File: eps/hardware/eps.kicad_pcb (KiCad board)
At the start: 4 copper layers, 80 x 80 mm, 401 parts, among them J1 USB_C_Receptacle_USB2.0_16P, J10 Conn_02x20_Counter_Clockwise, J11 Conn_01x03, J12 Conn_01x03, J13 Conn_ARM_JTAG_SWD_10, J2 Conn_01x02, J3 Conn_01x02, J4 Conn_01x02, J5 Conn_01x02, J6 Conn_01x02, J7 Conn_01x02, J8 Conn_01x02, Q1 NMOS, Q10 IRLML0030, Q11 IRLML0030, Q12 IRLML0030, Q13 IRLML0030, Q14 IRLML0030, Q15 IRLML0030, Q16 IRLML0030, Q17 IRLML0030, Q18 IRLML0030, Q19 IRLML0030, Q2 NMOS, Q20 IRLML0030, Q3 NMOS, Q4 NMOS, Q5 IRLML0030, Q6 IRLML0030, Q7 IRLML0030, Q8 IRLML0030, Q9 IRLML0030, SW1 SW_Push, SW2 SW_SPDT, U1 TPS22810DRV, U10 STM32L496ZGTx, U11 NCS214RSQT2G, U12 74LVC1G07SE-7, U14 TPS22810DRVT, U15 NCS214RSQT2G, U16 74LVC1G07SE-7, U18 TPS22810DRVT, U19 NCS214RSQT2G, U2 LTC3130-1, U20 74LVC1G07SE-7, U22 TPS22810DRVT, U23 NCS214RSQT2G, U24 74LVC1G07SE-7, U26 TPS22810DRVT, U27 NCS214RSQT2G, U28 74LVC1G07SE-7, U3 LTC4162-L, U30 TPS22810DRVT, U31 NCS214RSQT2G, U32 74LVC1G07SE-7, U34 TPS22810DRVT, U35 NCS214RSQT2G, U36 74LVC1G07SE-7, U38 TPS22810DRVT, U39 MP28167-A, U4 LTC4162-L, U40 MP28167-A, U41 LTC4415, U42 LTC4415, U5 NCS214RSQT2G, U6 74LVC1G07SE-7, U8 TPS22810DRVT, U9 TPS35-Q1, Y1 8MHz, Y2 32KHz

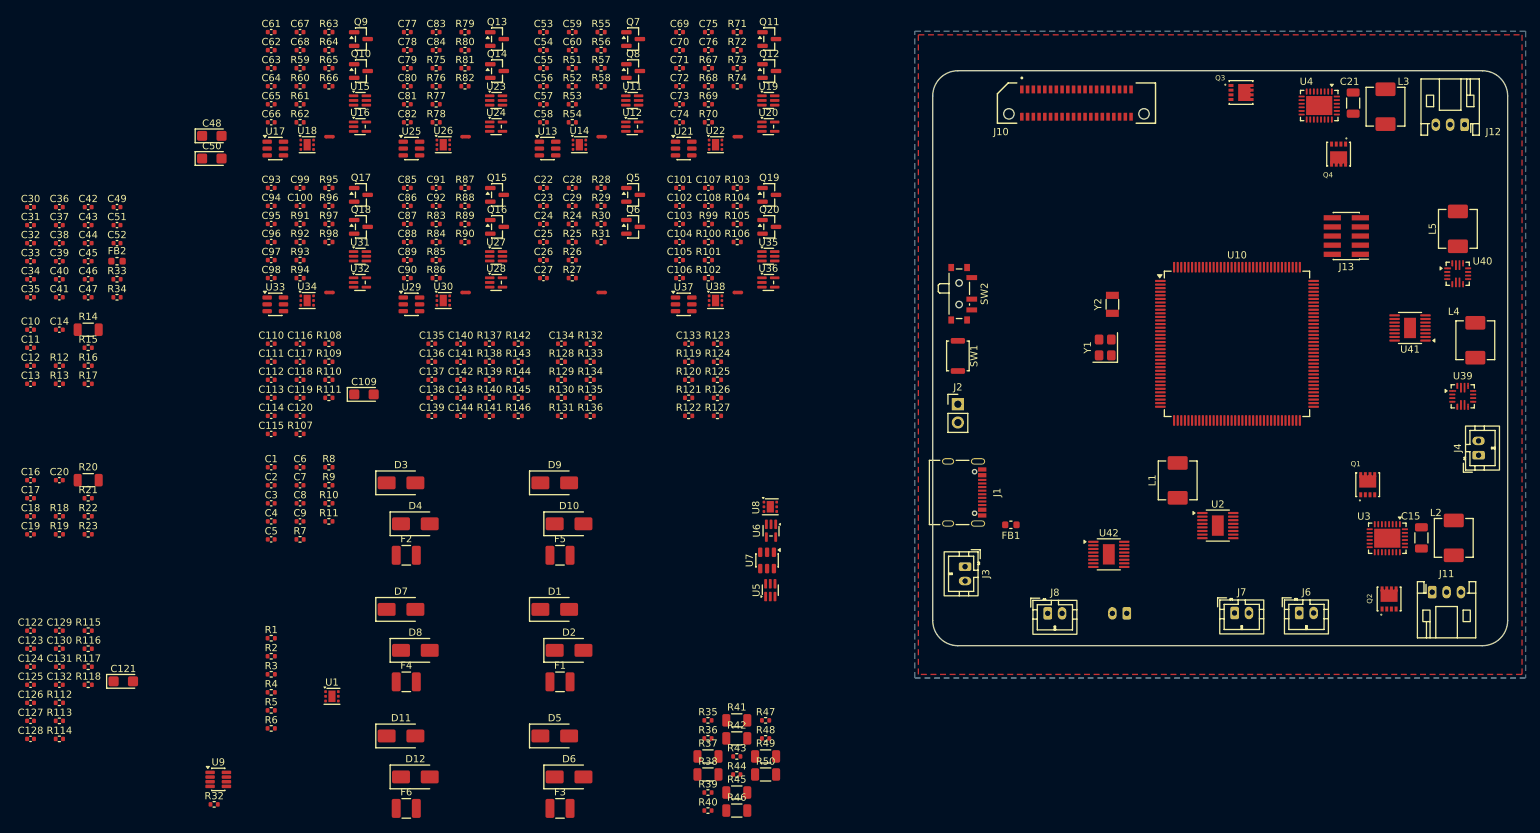
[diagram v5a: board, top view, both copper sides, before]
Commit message: start placement of one current monitor
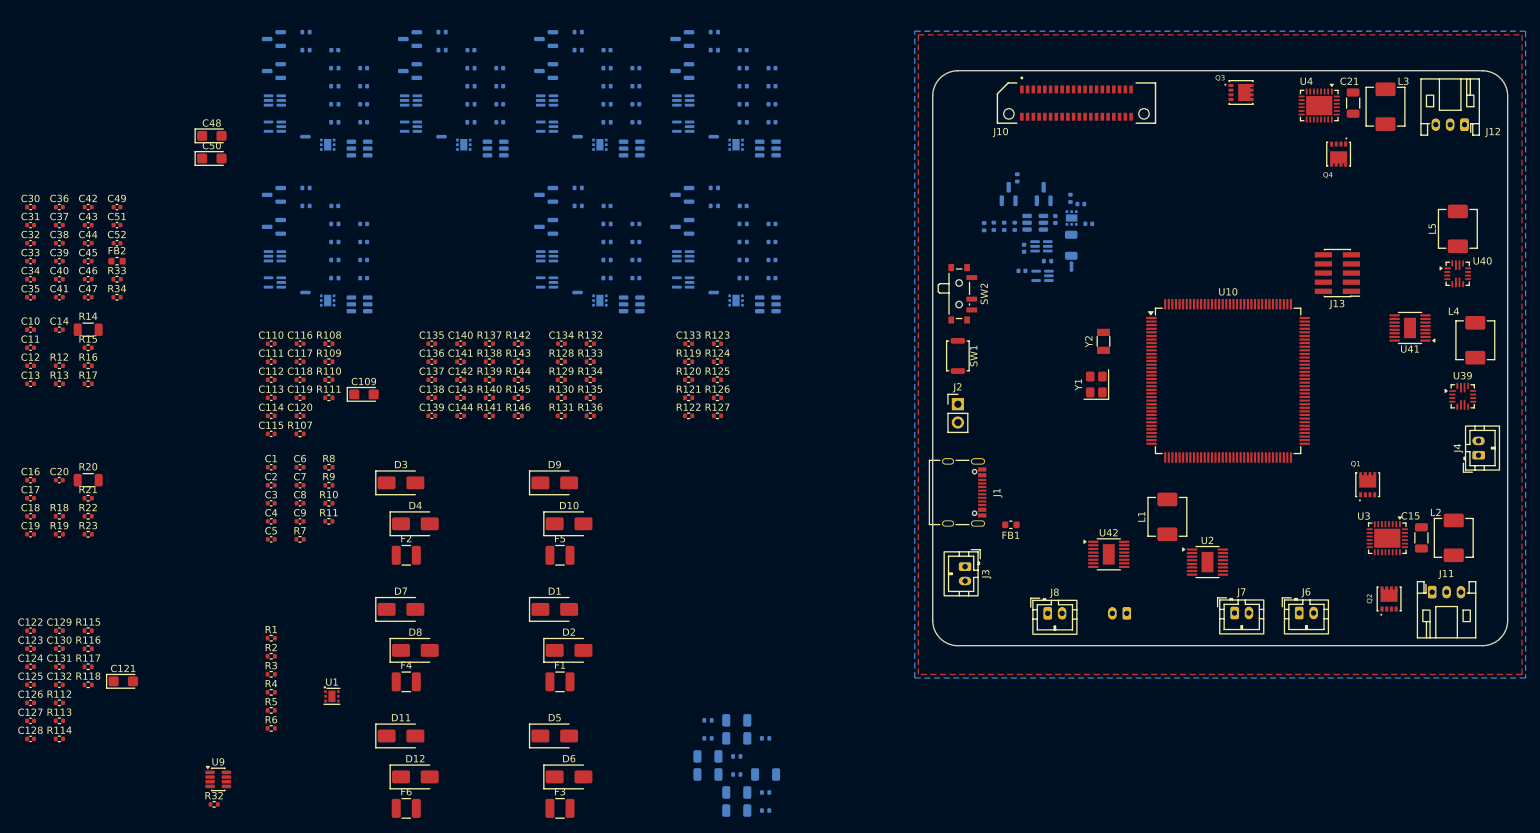
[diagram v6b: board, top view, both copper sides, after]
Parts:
- removed C101, C102, C107, C22, C23, C28, C53, C54, C59, C61, C62, C67, C69, C70, C75, C77, C78, C83, C85, C86, C91, C93, C94, C99: ~, Capacitor_SMD:C_0402_1005Metric
- removed R105, R106, R30, R31, R57, R58, R65, R66, R73, R74, R81, R82, R89, R90, R97, R98: 0, Resistor_SMD:R_0402_1005Metric
- C100, C103, C104, C105, C106, C108, C24, C25, C26, C27, C29, C55, C56, C57, C58, C60, C63, C64, C65, C66, C68, C71, C72, C73, C74, C76, C79, C80, C81, C82, C84, C87, C88, C89, C90, C92, C95, C96, C97, C98, NT1, NT2, NT3, NT4, NT5, NT6, NT7, NT8, Q10, Q11, Q12, Q13, Q14, Q15, Q16, Q17, Q18, Q19, Q20, Q5, Q6, Q7, Q8, Q9, R100, R101, R102, R103, R104, R24, R25, R26, R27, R28, R29, R35, R36, R37, R38, R39, R40, R41, R42, R43, R44, R45, R46, R47, R48, R49, R50, R51, R52, R53, R54, R55, R56, R59, R60, R61, R62, R63, R64, R67, R68, R69, R70, R71, R72, R75, R76, R77, R78, R79, R80, R83, R84, R85, R86, R87, R88, R91, R92, R93, R94, R95, R96, R99, U11, U12, U13, U14, U15, U16, U17, U18, U19, U20, U21, U22, U23, U24, U25, U26, U27, U28, U29, U30, U31, U32, U33, U34, U35, U36, U37, U38, U5, U6, U7, U8: moved to B.Cu
- moved R37 87.3 mm to (180.3, 76.3), turned to 90 degrees
- moved R35 80.9 mm to (172.4, 73.7), turned to -90 degrees
- moved C27 75.5 mm to (181.6, 70.5), turned to 180 degrees
- moved C29 71.9 mm to (182.7, 73.3), turned to 180 degrees
- moved C26 71.5 mm to (178.1, 72.7), turned to 90 degrees
- moved C63 69.7 mm to (138.6, 51.6), turned to 180 degrees
- moved C64 69.7 mm to (138.6, 54.1), turned to 180 degrees
- moved C65 69.7 mm to (138.6, 56.7), turned to 180 degrees
- moved C66 69.7 mm to (138.6, 59.2), turned to 180 degrees
- moved C95 69.7 mm to (138.6, 73.3), turned to 180 degrees
- moved C96 69.7 mm to (138.6, 75.8), turned to 180 degrees
- moved C97 69.7 mm to (138.6, 78.3), turned to 180 degrees
- moved C98 69.7 mm to (138.6, 80.8), turned to 180 degrees
- moved Q11 68.9 mm to (69.3, 47.6), turned to 180 degrees
- moved Q12 68.9 mm to (69.3, 52.0), turned to 180 degrees
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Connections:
- C103 pad 1: Net-(U37-VDD) -> /Current Monitors/RAIL_8_VOUT
- C104 pad 2: Net-(U37-VDD) -> /Current Monitors/RAIL_8_VOUT
- C24 pad 1: Net-(U7-VDD) -> /Current Monitors/RAIL_1_VOUT
- C25 pad 2: Net-(U7-VDD) -> /Current Monitors/RAIL_1_VOUT
- C55 pad 1: Net-(U13-VDD) -> /Current Monitors/RAIL_2_VOUT
- C56 pad 2: Net-(U13-VDD) -> /Current Monitors/RAIL_2_VOUT
- C63 pad 1: Net-(U17-VDD) -> /Current Monitors/RAIL_3_VOUT
- C64 pad 2: Net-(U17-VDD) -> /Current Monitors/RAIL_3_VOUT
- C71 pad 1: Net-(U21-VDD) -> /Current Monitors/RAIL_4_VOUT
- C72 pad 2: Net-(U21-VDD) -> /Current Monitors/RAIL_4_VOUT
- C79 pad 1: Net-(U25-VDD) -> /Current Monitors/RAIL_5_VOUT
- C80 pad 2: Net-(U25-VDD) -> /Current Monitors/RAIL_5_VOUT
- C87 pad 1: Net-(U29-VDD) -> /Current Monitors/RAIL_6_VOUT
- C88 pad 2: Net-(U29-VDD) -> /Current Monitors/RAIL_6_VOUT
- C95 pad 1: Net-(U33-VDD) -> /Current Monitors/RAIL_7_VOUT
- C96 pad 2: Net-(U33-VDD) -> /Current Monitors/RAIL_7_VOUT
- R139 pad 1: /Current Monitors/RAIL_1_ADC -> GND
- R140 pad 1: /Current Monitors/RAIL_2_ADC -> GND
- R141 pad 1: /Current Monitors/RAIL_3_ADC -> GND
- R142 pad 1: /Current Monitors/RAIL_4_ADC -> GND
- R143 pad 1: /Current Monitors/RAIL_5_ADC -> GND
- R144 pad 1: /Current Monitors/RAIL_6_ADC -> GND
- R145 pad 1: /Current Monitors/RAIL_7_ADC -> GND
- R146 pad 1: /Current Monitors/RAIL_8_ADC -> GND
- R24 pad 2: Net-(U7-VDD) -> /Current Monitors/RAIL_1_VOUT
- R51 pad 2: Net-(U13-VDD) -> /Current Monitors/RAIL_2_VOUT
- R59 pad 2: Net-(U17-VDD) -> /Current Monitors/RAIL_3_VOUT
- R67 pad 2: Net-(U21-VDD) -> /Current Monitors/RAIL_4_VOUT
- R75 pad 2: Net-(U25-VDD) -> /Current Monitors/RAIL_5_VOUT
- R83 pad 2: Net-(U29-VDD) -> /Current Monitors/RAIL_6_VOUT
- R91 pad 2: Net-(U33-VDD) -> /Current Monitors/RAIL_7_VOUT
- R99 pad 2: Net-(U37-VDD) -> /Current Monitors/RAIL_8_VOUT
- U11 pad 6: /Current Monitors/RAIL_2_ADC -> GND
- U12 pad 5: Net-(U13-VDD) -> /Current Monitors/RAIL_2_VOUT
- U13 pad 3: /Current Monitors/RAIL_2_ADC -> GND
- U13 pad 6: Net-(U13-VDD) -> /Current Monitors/RAIL_2_VOUT
- U14 pad 2: Net-(U14-QOD) -> /Current Monitors/RAIL_2_VOUT
- U14 pad 3: Net-(U14-CT) -> GND
- U15 pad 6: /Current Monitors/RAIL_3_ADC -> GND
- U16 pad 5: Net-(U17-VDD) -> /Current Monitors/RAIL_3_VOUT
- U17 pad 3: /Current Monitors/RAIL_3_ADC -> GND
- U17 pad 6: Net-(U17-VDD) -> /Current Monitors/RAIL_3_VOUT
- U18 pad 2: Net-(U18-QOD) -> /Current Monitors/RAIL_3_VOUT
- U18 pad 3: Net-(U18-CT) -> GND
- U19 pad 6: /Current Monitors/RAIL_4_ADC -> GND
- U20 pad 5: Net-(U21-VDD) -> /Current Monitors/RAIL_4_VOUT
- U21 pad 3: /Current Monitors/RAIL_4_ADC -> GND
- U21 pad 6: Net-(U21-VDD) -> /Current Monitors/RAIL_4_VOUT
- U22 pad 2: Net-(U22-QOD) -> /Current Monitors/RAIL_4_VOUT
- U22 pad 3: Net-(U22-CT) -> GND
- U23 pad 6: /Current Monitors/RAIL_5_ADC -> GND
- U24 pad 5: Net-(U25-VDD) -> /Current Monitors/RAIL_5_VOUT
- U25 pad 3: /Current Monitors/RAIL_5_ADC -> GND
- U25 pad 6: Net-(U25-VDD) -> /Current Monitors/RAIL_5_VOUT
- U26 pad 2: Net-(U26-QOD) -> /Current Monitors/RAIL_5_VOUT
- U26 pad 3: Net-(U26-CT) -> GND
- U27 pad 6: /Current Monitors/RAIL_6_ADC -> GND
- U28 pad 5: Net-(U29-VDD) -> /Current Monitors/RAIL_6_VOUT
- U29 pad 3: /Current Monitors/RAIL_6_ADC -> GND
- U29 pad 6: Net-(U29-VDD) -> /Current Monitors/RAIL_6_VOUT
- U30 pad 2: Net-(U30-QOD) -> /Current Monitors/RAIL_6_VOUT
- U30 pad 3: Net-(U30-CT) -> GND
- U31 pad 6: /Current Monitors/RAIL_7_ADC -> GND
- U32 pad 5: Net-(U33-VDD) -> /Current Monitors/RAIL_7_VOUT
- U33 pad 3: /Current Monitors/RAIL_7_ADC -> GND
- U33 pad 6: Net-(U33-VDD) -> /Current Monitors/RAIL_7_VOUT
- U34 pad 2: Net-(U34-QOD) -> /Current Monitors/RAIL_7_VOUT
- U34 pad 3: Net-(U34-CT) -> GND
- U35 pad 6: /Current Monitors/RAIL_8_ADC -> GND
- U36 pad 5: Net-(U37-VDD) -> /Current Monitors/RAIL_8_VOUT
- U37 pad 3: /Current Monitors/RAIL_8_ADC -> GND
- U37 pad 6: Net-(U37-VDD) -> /Current Monitors/RAIL_8_VOUT
- U38 pad 2: Net-(U38-QOD) -> /Current Monitors/RAIL_8_VOUT
- U38 pad 3: Net-(U38-CT) -> GND
- U5 pad 6: /Current Monitors/RAIL_1_ADC -> GND
- U6 pad 5: Net-(U7-VDD) -> /Current Monitors/RAIL_1_VOUT
- U7 pad 3: /Current Monitors/RAIL_1_ADC -> GND
- U7 pad 6: Net-(U7-VDD) -> /Current Monitors/RAIL_1_VOUT
- U8 pad 2: Net-(U8-QOD) -> /Current Monitors/RAIL_1_VOUT
- U8 pad 3: Net-(U8-CT) -> GND

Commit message: add better current monitoring layout
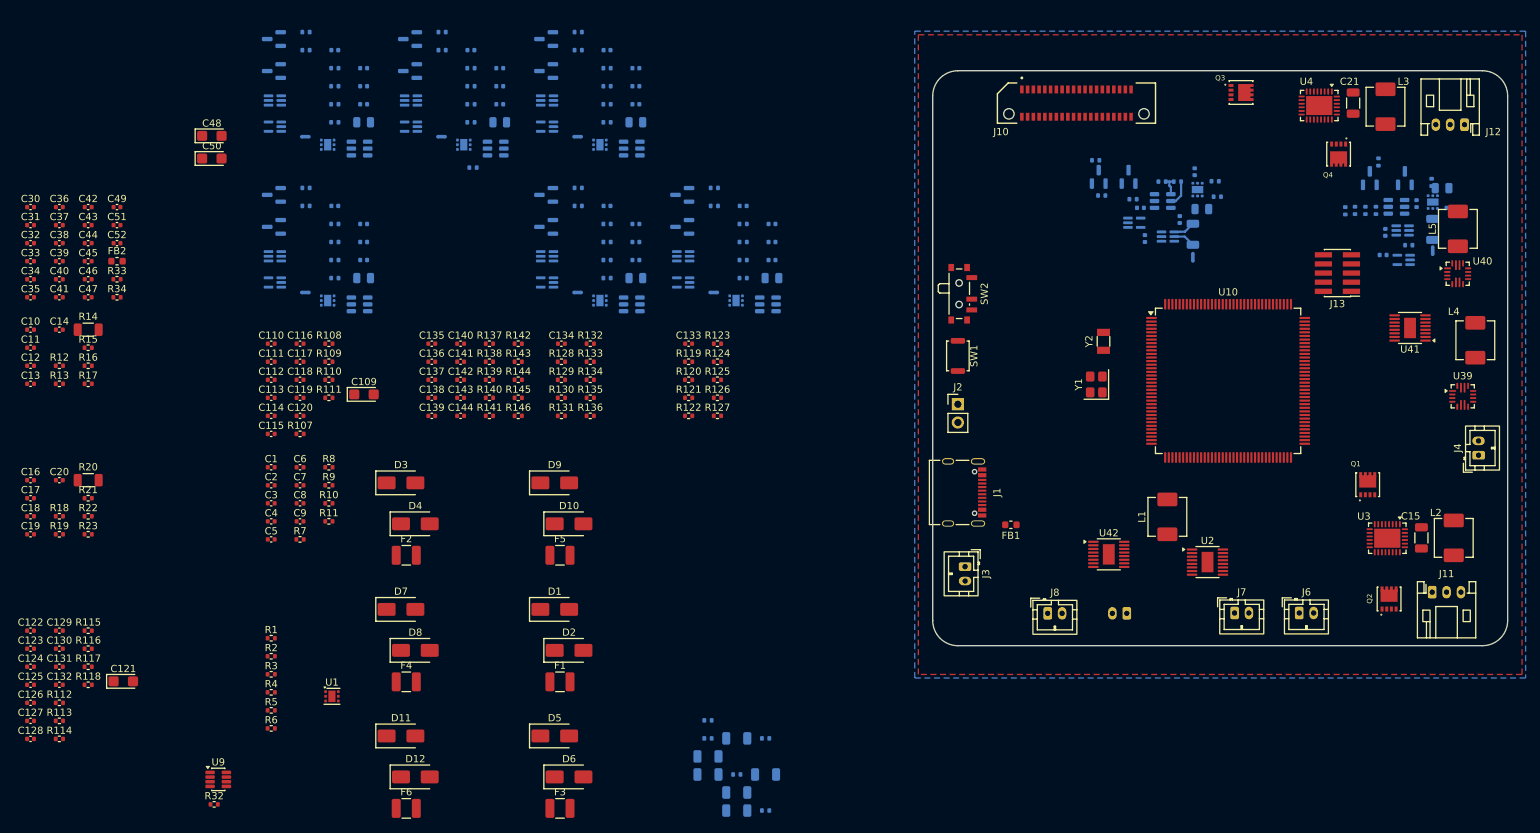
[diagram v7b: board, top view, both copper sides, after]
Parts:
- C106, C27, C58, C66, C74, C82, C90, C98: footprint Capacitor_SMD:C_0402_1005Metric -> Capacitor_SMD:C_0805_2012Metric
- moved R43 100.8 mm to (195.1, 67.4)
- moved R39 96.0 mm to (97.0, 65.5)
- moved R41 92.8 mm to (197.2, 74.8), turned to 90 degrees
- moved R64 72.9 mm to (200.6, 69.5)
- moved U15 70.1 mm to (193.7, 75.1), turned to 0 degrees
- moved NT3 68.8 mm to (197.2, 78.0), turned to 90 degrees
- moved R59 67.5 mm to (200.3, 67.4)
- moved C68 65.1 mm to (197.4, 66.0), turned to -90 degrees
- moved Q9 65.0 mm to (188.2, 66.8), turned to 90 degrees
- moved U18 64.5 mm to (197.8, 68.5), turned to -90 degrees
- moved U16 64.2 mm to (189.1, 73.2), turned to 0 degrees
- moved C66 61.0 mm to (198.4, 71.2)
- moved Q10 59.8 mm to (184.1, 66.8), turned to 90 degrees
- moved R60 59.8 mm to (192.9, 67.4)
- moved C64 59.7 mm to (195.4, 72.7), turned to 90 degrees
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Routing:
- net /Current Monitors/Sensors/RREF+: track 0.00 -> 3.68 mm
- net /Current Monitors/Sensors/Shunt-: track 0.00 -> 3.06 mm
- net /Current Monitors/Sensors/Shunt+: track 0.00 -> 3.06 mm
- net /Current Monitors/Sensors/RREF-: track 0.00 -> 2.95 mm
